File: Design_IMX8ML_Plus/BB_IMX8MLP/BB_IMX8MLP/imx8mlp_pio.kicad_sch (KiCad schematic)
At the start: 10 parts, among them J1 DF40C-100DP-0.4V_51_, J2 DF40C-100DP-0.4V_51_, J3 DF40C-100DP-0.4V_51_, J4 DF40C-100DP-0.4V_51_

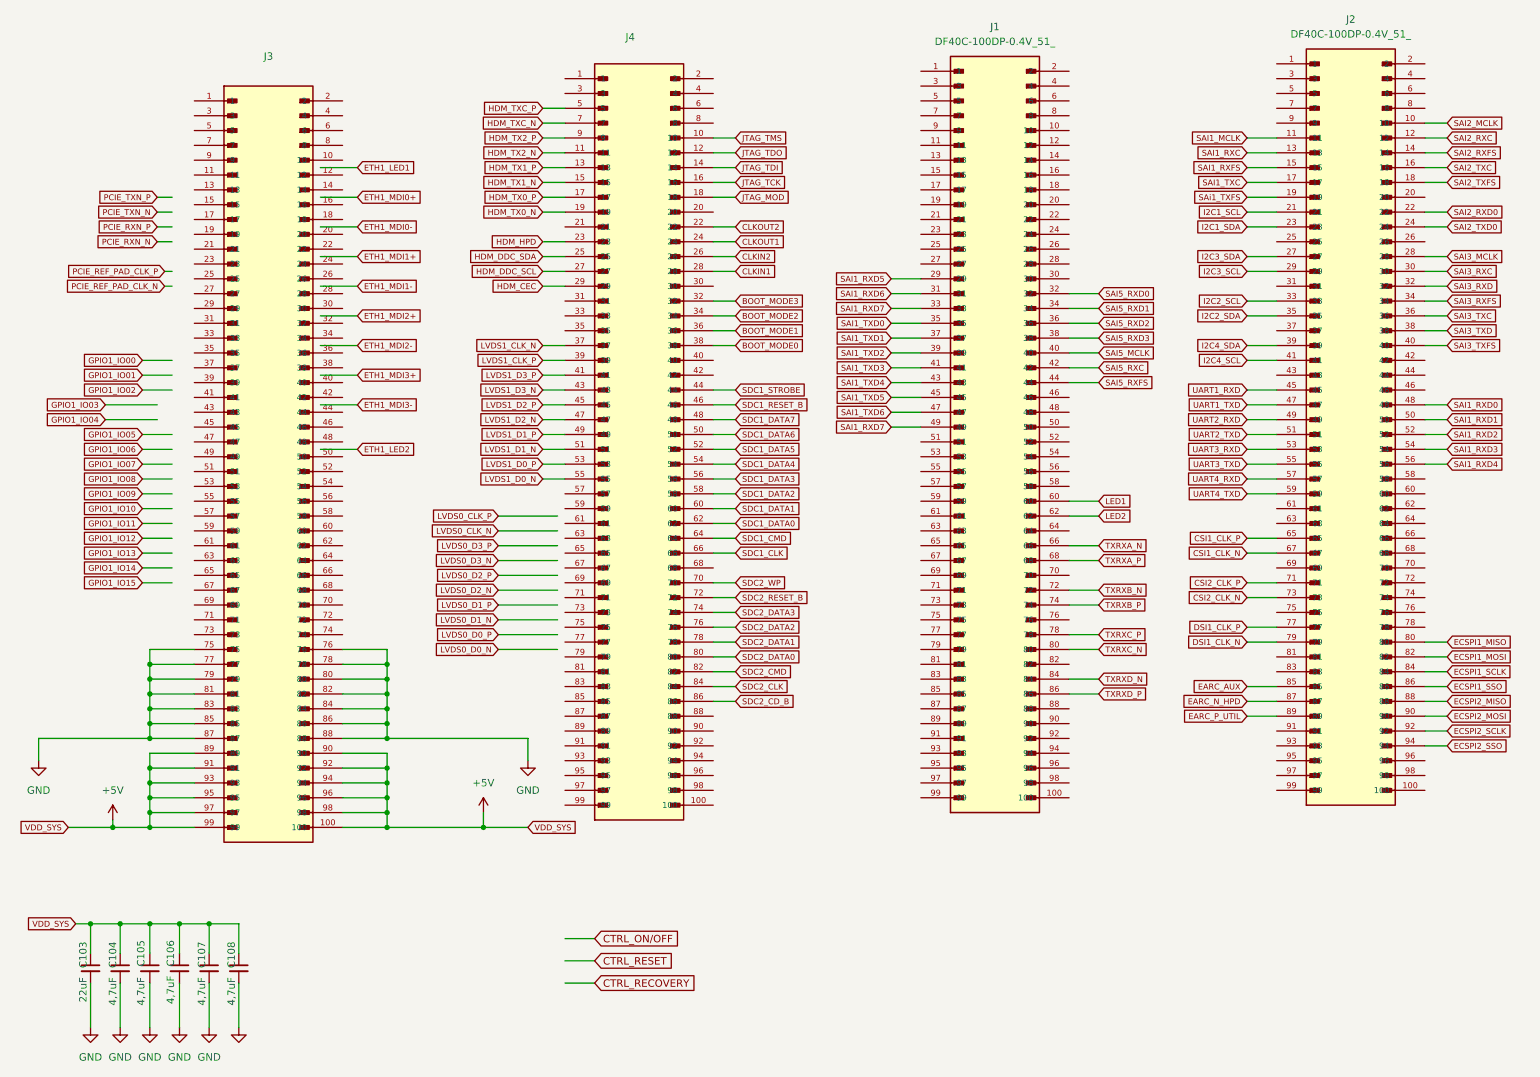
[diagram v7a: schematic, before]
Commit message: [PROCESSOR] Create zones It added power zones in the four layer
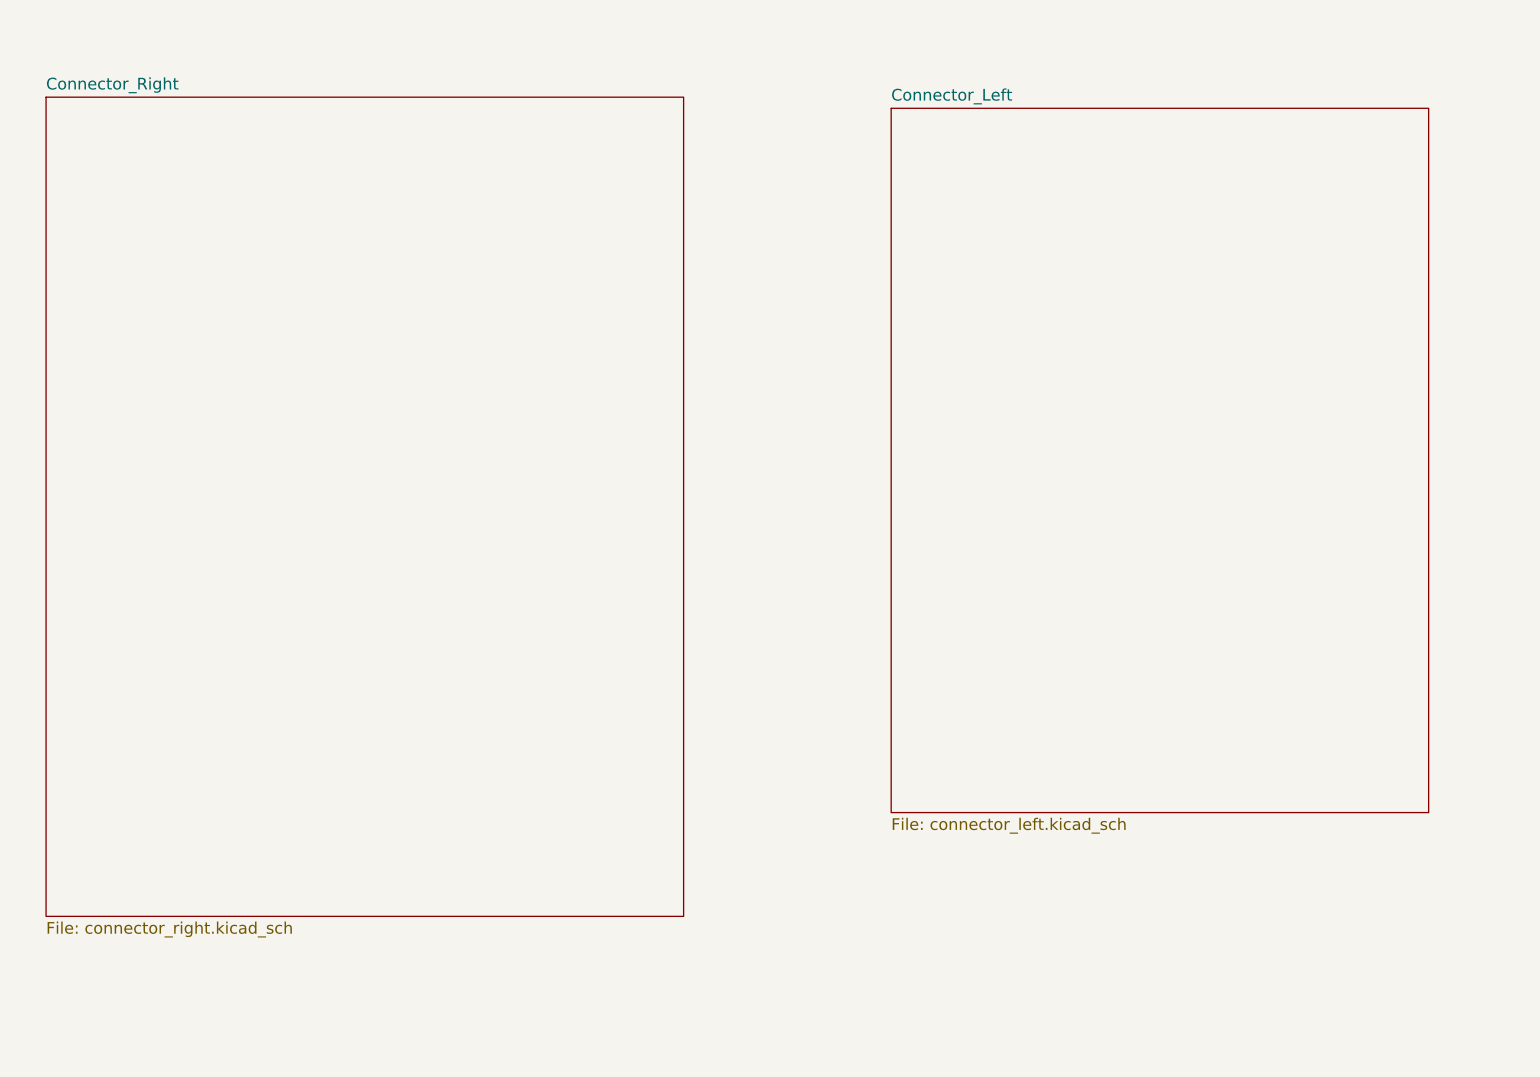
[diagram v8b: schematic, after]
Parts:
- removed C103: 22uF, Capacitor_SMD:C_0402_1005Metric, symbol Device:C_Small
- removed C104, C105, C106, C107, C108: 4,7uF, Capacitor_SMD:C_0402_1005Metric, symbol Device:C_Small
- removed J1, J2, J4: DF40C-100DP-0.4V_51_, _W_SBC:HIROSE_DF40C-100DS-0.4V_51_, symbol CONN_DF40C-100DS-0_4V51_HIR:DF40C-100DP-0.4V_51_
- removed J3: DF40C-100DP-0.4V_51_, _W_SBC:HIROSE_DF40C-100DS-0.4V_51_, symbol df40c-100dp-0.4v_51_:DF40C-100DP-0.4V_51_
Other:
- added sheet Connector_Left (connector_left.kicad_sch)
- added sheet Connector_Right (connector_right.kicad_sch)
